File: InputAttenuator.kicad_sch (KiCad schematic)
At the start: 7 parts

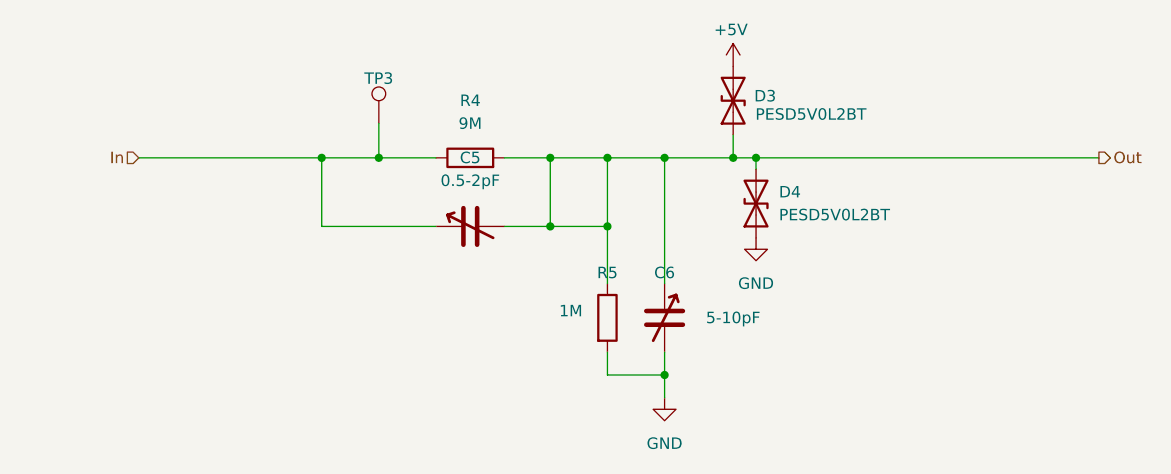
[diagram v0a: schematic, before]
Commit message: DRC completed. Need to add some 3D models.
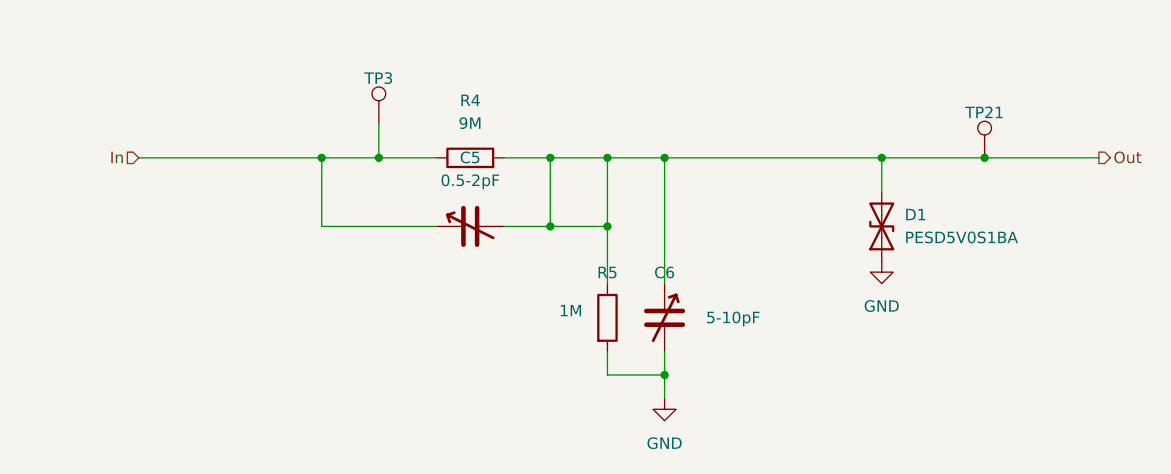
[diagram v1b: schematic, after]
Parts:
- removed D3, D4: PESD5V0L2BT, Diode_SMD:D_SOD-882, symbol Device:D_TVS
- added D1: PESD5V0S1BA, Diode_SMD:D_SOD-323_HandSoldering, symbol Device:D_TVS
- added TP21: TP, TestPoint:TestPoint_Pad_D1.0mm, symbol Connector:TestPoint
- C5, C6: footprint Capacitor_SMD:C_Trimmer_Murata_TZB4-B -> Capacitor_SMD:C_Trimmer_Murata_TZC3
- R4, R5: footprint Resistor_SMD:R_0805_2012Metric -> Resistor_SMD:R_0603_1608Metric_Pad0.98x0.95mm_HandSolder
- TP3: footprint TestPoint:TestPoint_Pad_D2.0mm -> TestPoint:TestPoint_Pad_D1.0mm
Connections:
- net GND: now also D1.1 (A1)
- net Out: now also D1.2 (A2), TP21.1

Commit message: R1 sent to JLCPCB
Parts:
- added R7: 5M1, Resistor_SMD:R_0603_1608Metric_Pad0.98x0.95mm_HandSolder, symbol Device:R
- C5, C6: JLCPCB# (none) -> C22468120
- D1: JLCPCB# (none) -> C2827694
- R4: value 9M -> 3M9; JLCPCB# (none) -> C423039
- R5: JLCPCB# (none) -> C4165581
- TP21, TP3: now left out of the parts list
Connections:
- net In: now also R7.1; no longer R4.1
- new net: R4.1, R7.2
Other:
- moved on the sheet: TP3
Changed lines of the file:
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@@
 	)
 	(junction
-		(at 111.76 90.17)
+		(at 102.87 90.17)
 		(diameter 0)
 		(color 0 0 0 0)
@@
 	)
 	(junction
-		(at 105.41 90.17)
+		(at 96.52 90.17)
 		(diameter 0)
 		(color 0 0 0 0)
@@
 	(wire
 		(pts
-			(xy 85.09 90.17) (xy 105.41 90.17)
-		)
-		(stroke
-			(width 0)
-			(type default)
-		)
-	)
-	(wire
-		(pts
-			(xy 105.41 90.17) (xy 105.41 97.79)
+			(xy 76.2 90.17) (xy 96.52 90.17)
+		)
+		(stroke
+			(width 0)
+			(type default)
+		)
+	)
+	(wire
+		(pts
+			(xy 96.52 90.17) (xy 96.52 97.79)
 		)
 		(stroke
@@
 	(wire
 		(pts
-			(xy 105.41 90.17) (xy 111.76 90.17)
+			(xy 96.52 90.17) (xy 102.87 90.17)
 		)
 		(stroke
@@
 	(wire
 		(pts
+			(xy 114.3 90.17) (xy 118.11 90.17)
+		)
+		(stroke
+			(width 0)
+			(type default)
+		)
+	)
+	(wire
+		(pts
 			(xy 125.73 90.17) (xy 130.81 90.17)
 		)
@@
 	(wire
 		(pts
-			(xy 111.76 90.17) (xy 118.11 90.17)
-		)
-		(stroke
-			(width 0)
-			(type default)
-		)
-	)
-	(wire
-		(pts
-			(xy 105.41 97.79) (xy 118.11 97.79)
+			(xy 102.87 90.17) (xy 106.68 90.17)
+		)
+		(stroke
+			(width 0)
+			(type default)
+		)
+	)
+	(wire
+		(pts
+			(xy 96.52 97.79) (xy 118.11 97.79)
 		)
 		(stroke
@@
 	(wire
 		(pts
-			(xy 111.76 86.36) (xy 111.76 90.17)
+			(xy 102.87 86.36) (xy 102.87 90.17)
 		)
 		(stroke
@@
 	(hierarchical_label "In"
 		(shape input)
-		(at 85.09 90.17 180)
+		(at 76.2 90.17 180)
 		(effects
 			(font
@@
 	(symbol
 		(lib_id "Connector:TestPoint")
-		(at 111.76 86.36 0)
+		(at 102.87 86.36 0)
 		(unit 1)
 		(exclude_from_sim no)
-		(in_bom yes)
+		(in_bom no)
 		(on_board yes)
 		(dnp no)
 		(property "Reference" "TP3"
-			(at 111.76 81.36 0)
+			(at 102.87 81.36 0)
 			(effects
 				(font
@@
 		)
 		(property "Value" "TP"
-			(at 113.538 85.344 0)
+			(at 104.648 85.344 0)
 			(effects
 				(font
@@
 		)
 		(property "Footprint" "TestPoint:TestPoint_Pad_D1.0mm"
-			(at 111.76 93.36 0)
+			(at 102.87 93.36 0)
 			(effects
 				(font
@@
 		)
 		(property "Datasheet" "~"
-			(at 111.76 86.36 0)
+			(at 102.87 86.36 0)
 			(effects
 				(font
@@
 		)
 		(property "Description" "Test point - Input positive"
-			(at 111.76 86.36 0)
+			(at 102.87 86.36 0)
+			(effects
+				(font
+					(size 1.27 1.27)
+				)
+				(hide yes)
+			)
+		)
+		(property "JLCPCB#" ""
+			(at 102.87 86.36 0)
 			(effects
 				(font
@@
 			)
 		)
+		(property "JLCPCB#" "C2827694"
+			(at 167.64 97.79 90)
+			(effects
+				(font
+					(size 1.27 1.27)
+				)
+				(hide yes)
+			)
+		)
 		(pin "2"
 		)
@@
 		(on_board yes)
 		(dnp no)
-		(fields_autoplaced yes)
 		(property "Reference" "C5"
-			(at 121.92 90.17 90)
+			(at 121.666 94.234 90)
 			(effects
 				(font
@@
 		)
 		(property "Value" "0.5-2pF"
-			(at 121.92 92.71 90)
+			(at 121.666 101.6 90)
 			(effects
 				(font
@@
 		(property "Type" "NP0/C0G"
 			(at 121.92 97.79 0)
+			(effects
+				(font
+					(size 1.27 1.27)
+				)
+				(hide yes)
+			)
+		)
+		(property "JLCPCB#" "C22468120"
+			(at 121.92 97.79 90)
 			(effects
 				(font
@@
 			)
 		)
-		(property "Value" "9M"
+		(property "Value" "3M9"
 			(at 121.92 86.36 90)
 			(effects
@@
 		(property "Type" "Thin film"
 			(at 121.92 90.17 0)
+			(effects
+				(font
+					(size 1.27 1.27)
+				)
+				(hide yes)
+			)
+		)
+		(property "JLCPCB#" "C423039"
+			(at 121.92 90.17 90)
 			(effects
 				(font
@@
 			)
 		)
+		(property "JLCPCB#" "C22468120"
+			(at 143.51 107.95 0)
+			(effects
+				(font
+					(size 1.27 1.27)
+				)
+				(hide yes)
+			)
+		)
 		(pin "1"
 		)
@@
 		)
 		(property "Type" "Thin film"
+			(at 137.16 107.95 0)
+			(effects
+				(font
+					(size 1.27 1.27)
+				)
+				(hide yes)
+			)
+		)
+		(property "JLCPCB#" "C4165581"
 			(at 137.16 107.95 0)
 			(effects
@@
 	)
 	(symbol
-		(lib_id "Connector:TestPoint")
-		(at 179.07 90.17 0)
+		(lib_id "Device:R")
+		(at 110.49 90.17 90)
 		(unit 1)
 		(exclude_from_sim no)
@@
 		(on_board yes)
 		(dnp no)
+		(fields_autoplaced yes)
+		(property "Reference" "R7"
+			(at 110.49 83.82 90)
+			(effects
+				(font
+					(size 1.27 1.27)
+				)
+			)
+		)
+		(property "Value" "5M1"
+			(at 110.49 86.36 90)
+			(effects
+				(font
+					(size 1.27 1.27)
+				)
+			)
+		)
+		(property "Footprint" "Resistor_SMD:R_0603_1608Metric_Pad0.98x0.95mm_HandSolder"
+			(at 117.49 90.17 0)
+			(effects
+				(font
+					(size 1.27 1.27)
+				)
+				(hide yes)
+			)
+		)
+		(property "Datasheet" "~"
+			(at 110.49 90.17 0)
+			(effects
+				(font
+					(size 1.27 1.27)
+				)
+				(hide yes)
+			)
+		)
+		(property "Description" "Input attenuator - positive channel"
+			(at 110.49 90.17 0)
+			(effects
+				(font
+					(size 1.27 1.27)
+				)
+				(hide yes)
+			)
+		)
+		(property "Tolerance" "0.1%"
+			(at 110.49 90.17 0)
+			(effects
+				(font
+					(size 1.27 1.27)
+				)
+				(hide yes)
+			)
+		)
+		(property "Type" "Thin film"
+			(at 110.49 90.17 0)
+			(effects
+				(font
+					(size 1.27 1.27)
+				)
+				(hide yes)
+			)
+		)
+		(property "JLCPCB#" "C13320"
+			(at 110.49 90.17 90)
+			(effects
+				(font
+					(size 1.27 1.27)
+				)
+				(hide yes)
+			)
+		)
+		(pin "1"
+		)
+		(pin "2"
+		)
+		(instances
+			(project "active-diff"
+				(path "/f9dd9bc6-979c-4d28-bd04-976faf1f4f50/50c10b95-8dc6-4894-a9d4-6edbe8eb0a19"
+					(reference "R16")
+					(unit 1)
+				)
+				(path "/f9dd9bc6-979c-4d28-bd04-976faf1f4f50/6d95b8ad-c228-4248-8435-ba4ae435dc6d"
+					(reference "R7")
+					(unit 1)
+				)
+			)
+		)
+	)
+	(symbol
+		(lib_id "Connector:TestPoint")
+		(at 179.07 90.17 0)
+		(unit 1)
+		(exclude_from_sim no)
+		(in_bom no)
+		(on_board yes)
+		(dnp no)
 		(property "Reference" "TP21"
 			(at 179.07 85.17 0)
@@
 			(at 179.07 90.17 0)
 			(effects
+				(font
+					(size 1.27 1.27)
+				)
+				(hide yes)
+			)
+		)
+		(property "JLCPCB#" ""
+			(at 179.07 90.17 0)
+			(effects
